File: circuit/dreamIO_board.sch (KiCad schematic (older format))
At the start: 78 parts, among them IC1 TPS61200, P1 BATT, P2 CONN_01X08, P3 CONN_01X08, P4 CONN_01X02, P5 CONN_01X06, P6 gnd_con, P7 CONN_01X03, P8 NO_CASCADE, P9 PixelOut, SW1 SPDT, SW2 RESET, SW3 PRGM, SW4 HCI2, SW5 HCI1, U1 MCP73831, U17 MPU-6050, U2 MICRO-B_USB, U3 UA78M33_SOT223, U4 ESP-12E

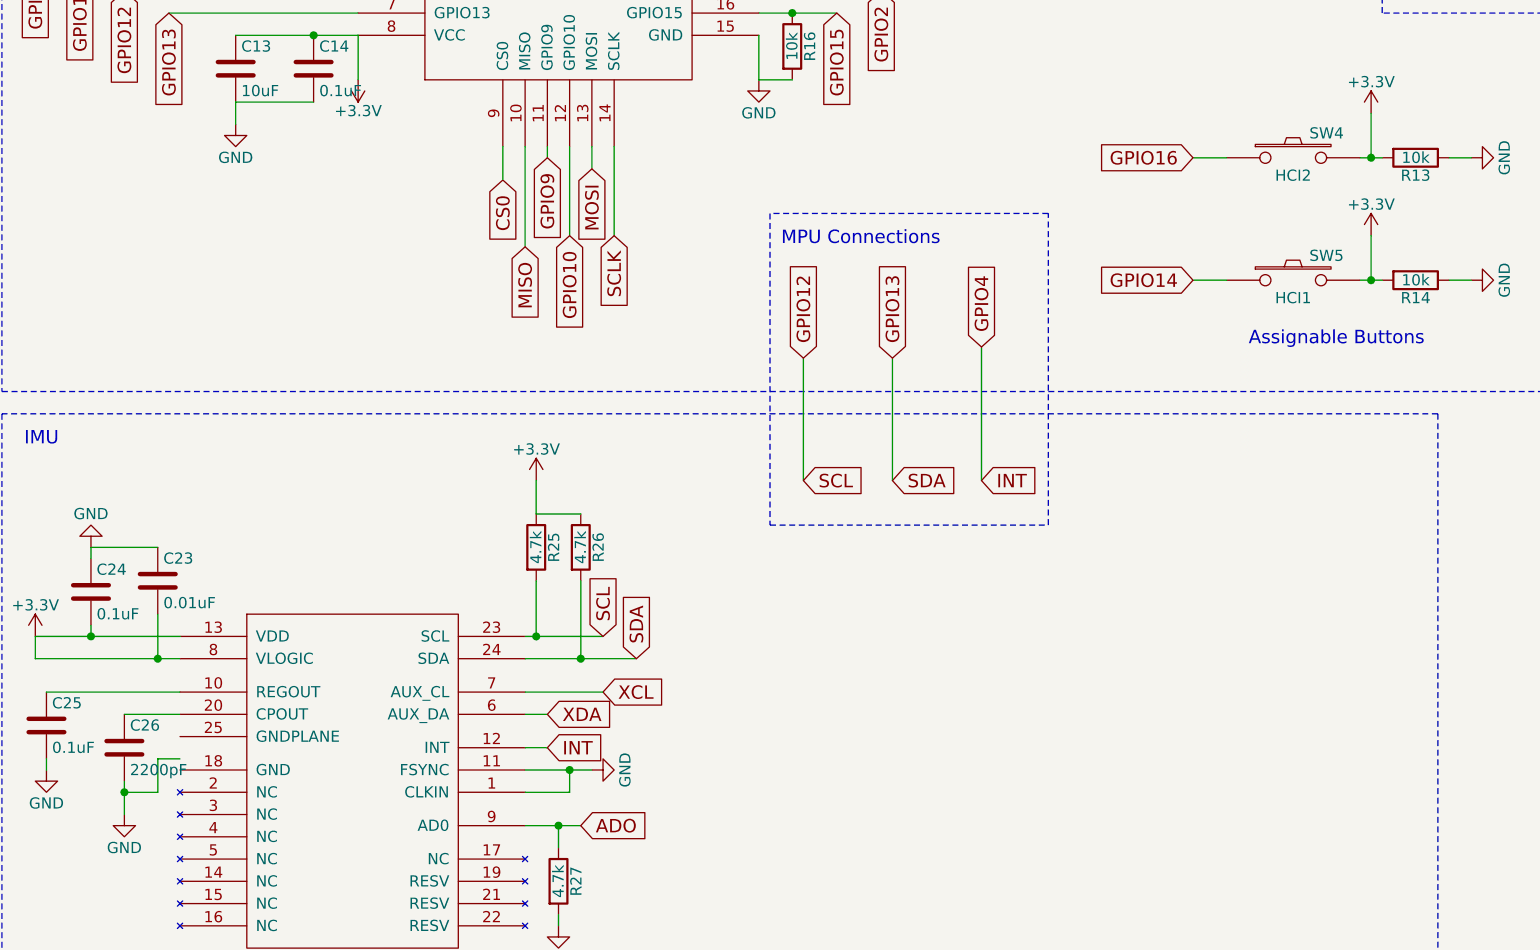
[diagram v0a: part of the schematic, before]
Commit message: changed pinout for MPU6050 to include groundplane under area. started on routing
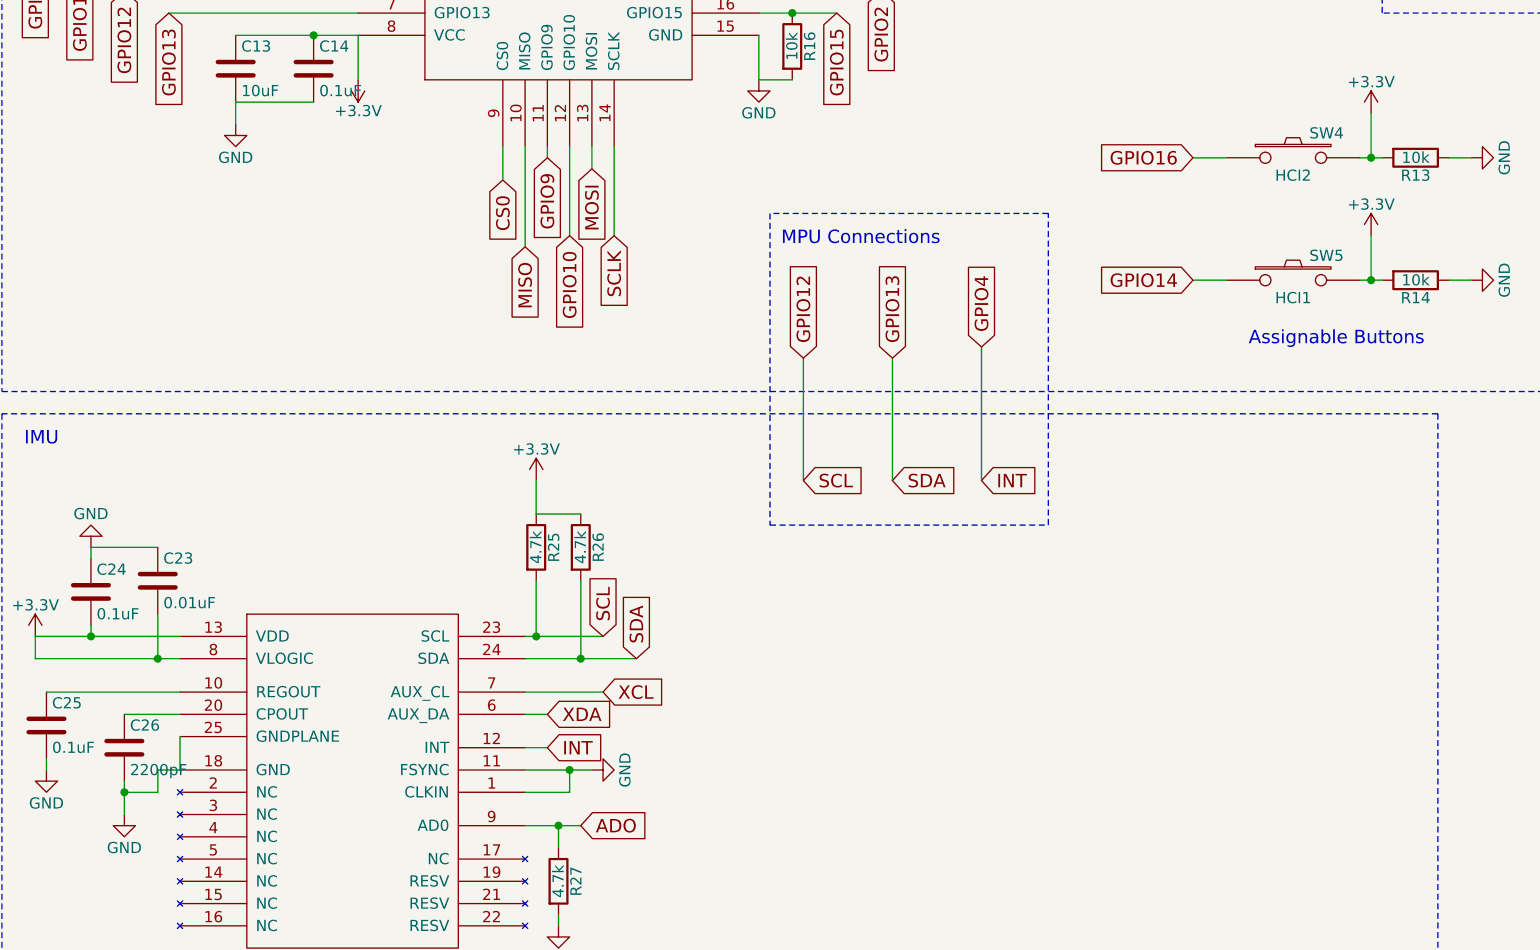
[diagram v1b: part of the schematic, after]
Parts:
- U17: footprint kicad-libraries:QFN-24-4x4-EP -> mpu6050:QFN-24-4x4-EP_steevedit
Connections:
- net GND: now also U17.18 (GND), U17.25 (GNDPLANE)
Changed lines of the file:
@@
 F 0 "U17" H 3150 11700 60  0000 C CNN
 F 1 "MPU-6050" H 2550 11700 60  0000 C CNN
-F 2 "kicad-libraries:QFN-24-4x4-EP" H 2800 12150 60  0001 C CNN
+F 2 "mpu6050:QFN-24-4x4-EP_steevedit" H 2800 12150 60  0001 C CNN
 F 3 "" H 2800 12150 60  0000 C CNN
 	1    2800 12400
@@
 	1900 12300 1750 12300
 Wire Wire Line
-	1900 12150 1900 12300
-Wire Wire Line
-	2000 12150 1900 12150
+	1900 12200 1900 12300
+Wire Wire Line
+	2000 12200 1900 12200
 Wire Wire Line
 	1750 12250 1750 12400
@@
 	7800 9450 7700 9450
 Wire Wire Line
-	7400 9450 7300 9450
+	7300 9450 7400 9450
 $Comp
 L +3.3V #PWR048
@@
 	7800 10000 7700 10000
 Wire Wire Line
-	7400 10000 7300 10000
+	7300 10000 7400 10000
 $Comp
 L +3.3V #PWR050
@@
 Text Notes 6750 2500 0    60   ~ 0
 in case no 3.3v reg
+Wire Wire Line
+	2000 12050 2000 12200
 $EndSCHEMATC

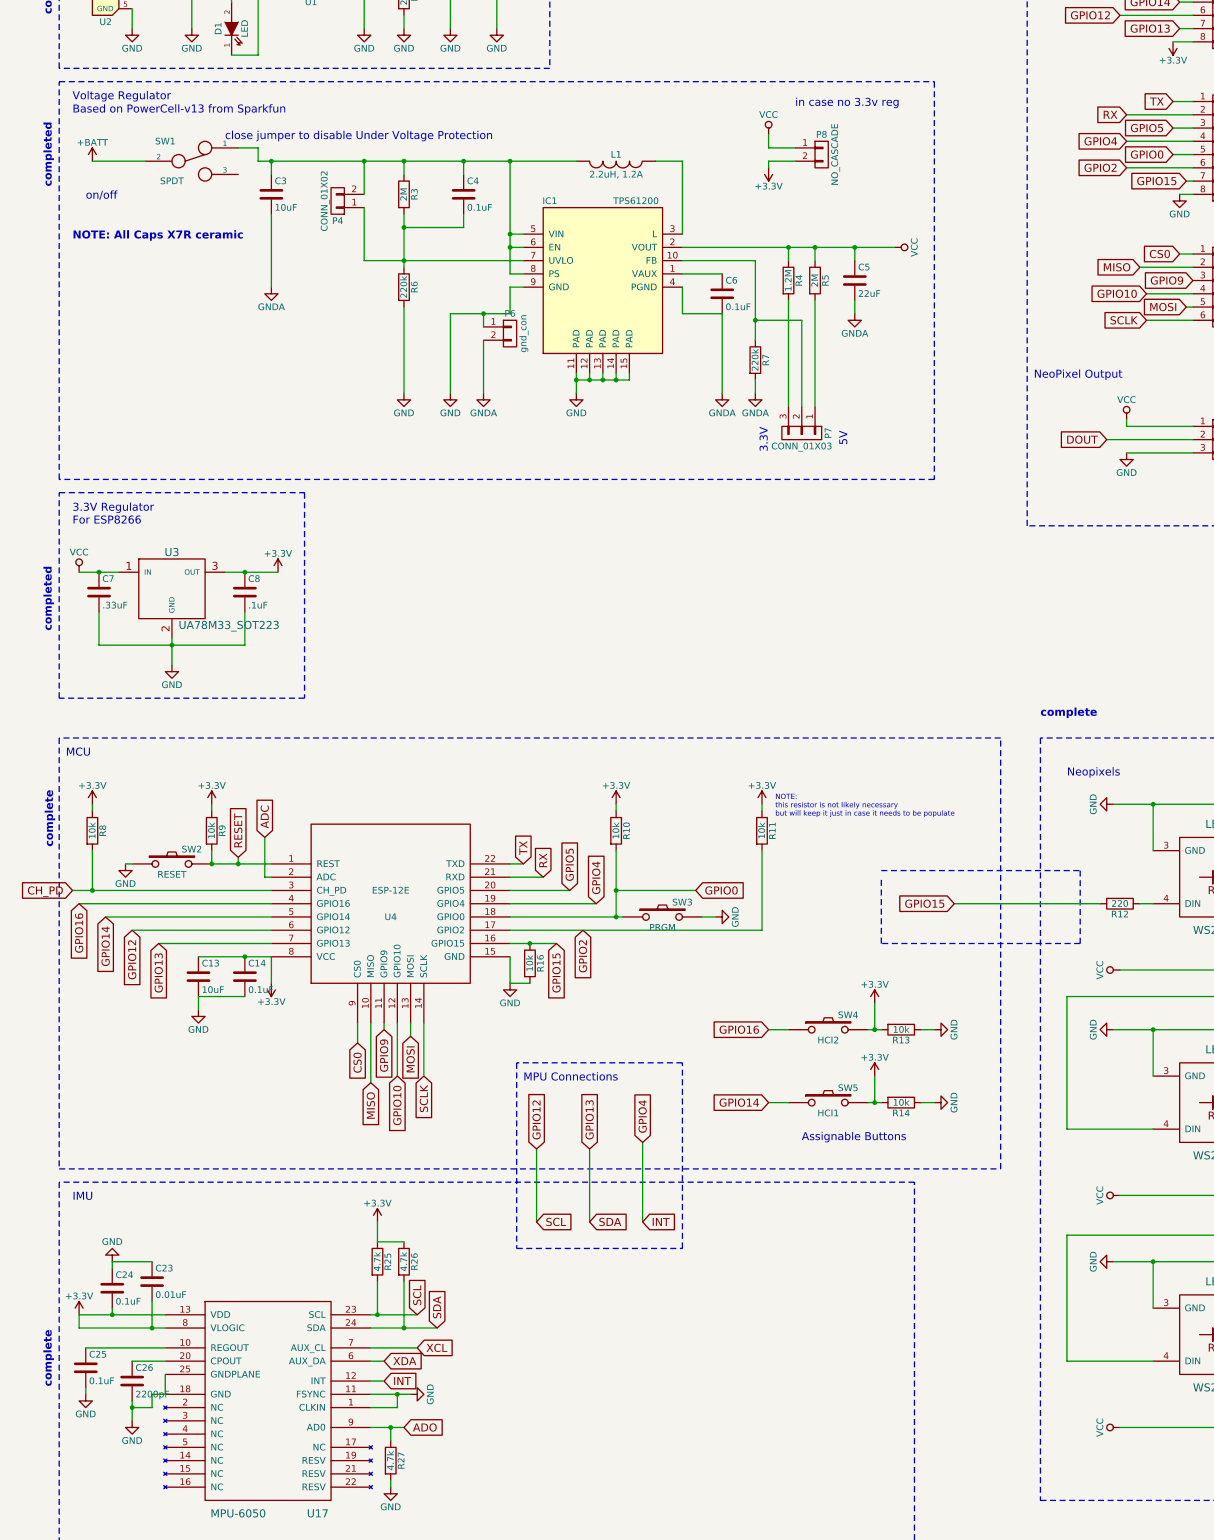
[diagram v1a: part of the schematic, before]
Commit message: removed the 3.3V regulator. The TPS61200 is now the main regulator and will be 5V.
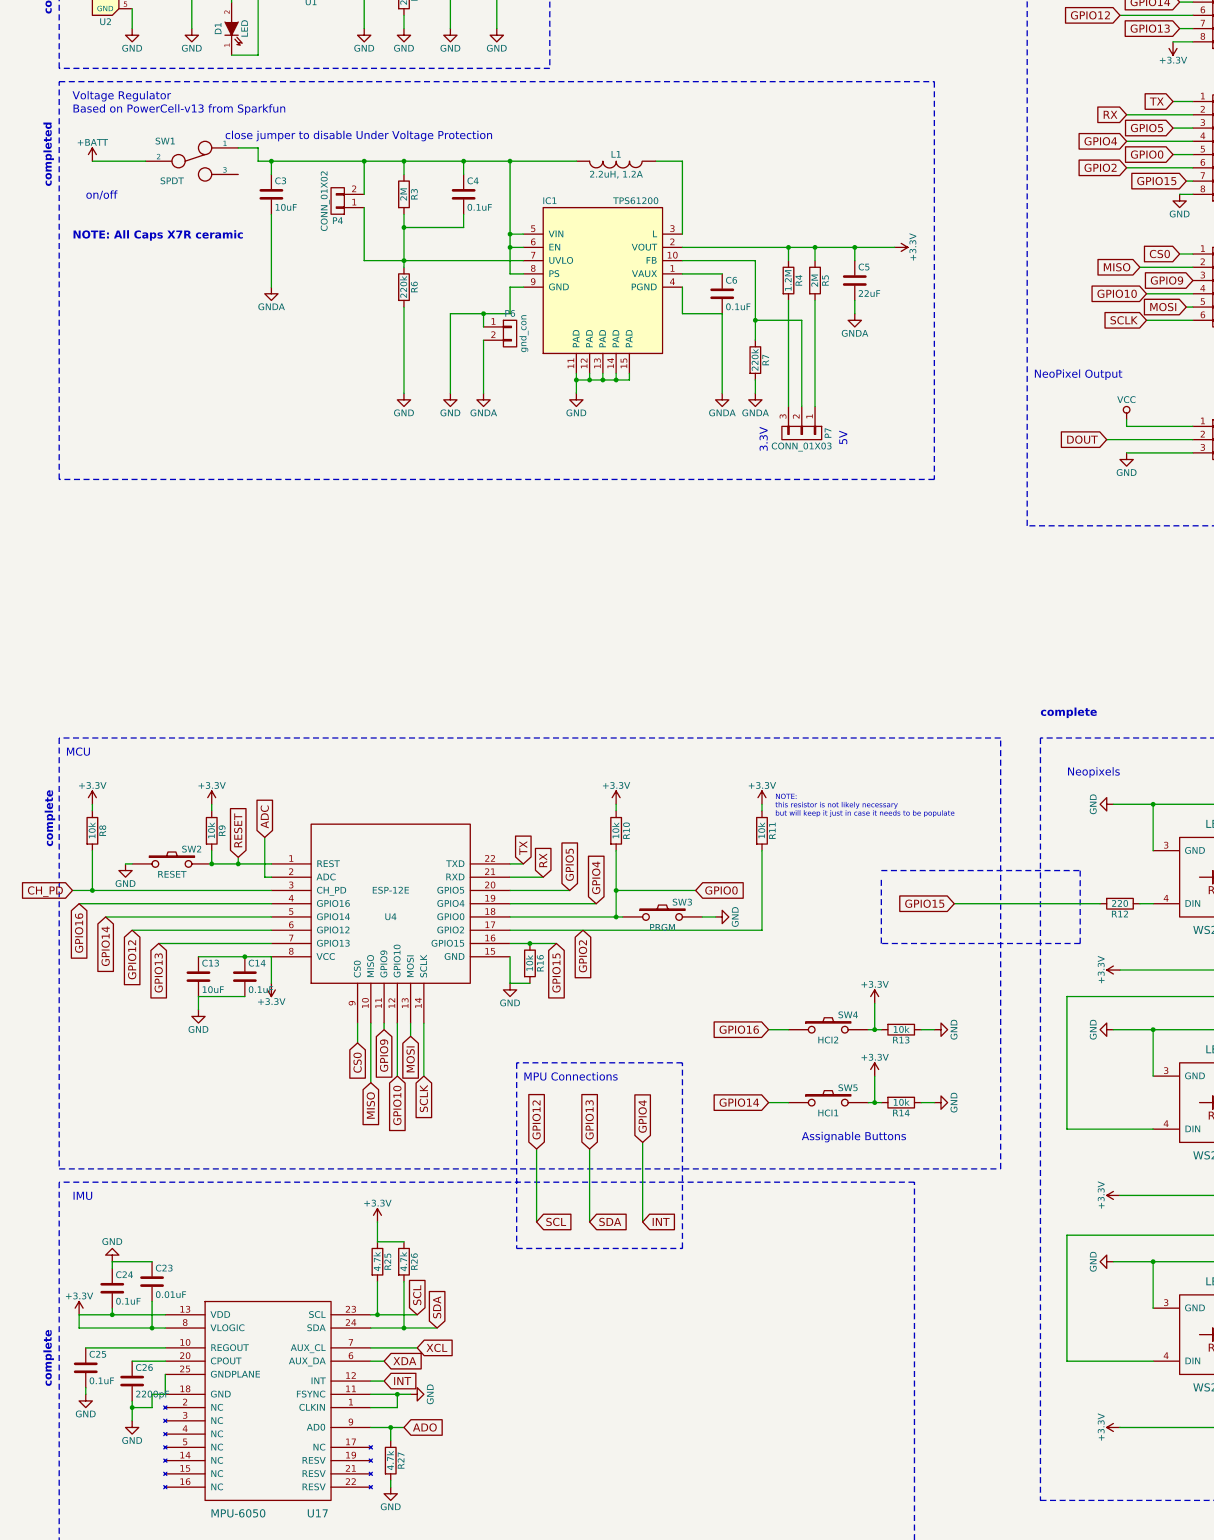
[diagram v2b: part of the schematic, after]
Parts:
- removed C7: .33uF, kicad-libraries:0603, symbol C
- removed C8: .1uF, kicad-libraries:0603, symbol C
- removed P8: NO_CASCADE, _connectors:_Solder_Pad2.54_2, symbol CONN_01X02
- removed U3: UA78M33_SOT223, kicad-libraries:SOT-223, symbol UA78M33_SOT223
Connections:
- net +3V3: now also C10.2, C11.2, C12.2, C15.2, C16.2, C17.2, C18.2, C19.2, C20.2, C21.2, C22.2, C5.1, C9.2, IC1.2 (VOUT), LED1.1 (VCC), LED10.1 (VCC), LED11.1 (VCC), LED12.1 (VCC), LED2.1 (VCC), LED3.1 (VCC), LED4.1 (VCC), LED5.1 (VCC), LED6.1 (VCC), LED7.1 (VCC), LED8.1 (VCC), LED9.1 (VCC), R4.1, R5.1
- net VCC: no longer C10.2, C11.2, C12.2, C15.2, C16.2, C17.2, C18.2, C19.2, C20.2, C21.2, C22.2, C5.1, C9.2, IC1.2 (VOUT), LED1.1 (VCC), LED10.1 (VCC), LED11.1 (VCC), LED12.1 (VCC), LED2.1 (VCC), LED3.1 (VCC), LED4.1 (VCC), LED5.1 (VCC), LED6.1 (VCC), LED7.1 (VCC), LED8.1 (VCC), LED9.1 (VCC), R4.1, R5.1
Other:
- note removed: "3.3V Regulator\nFor ESP8266"
- note removed: "in case no 3.3v reg"

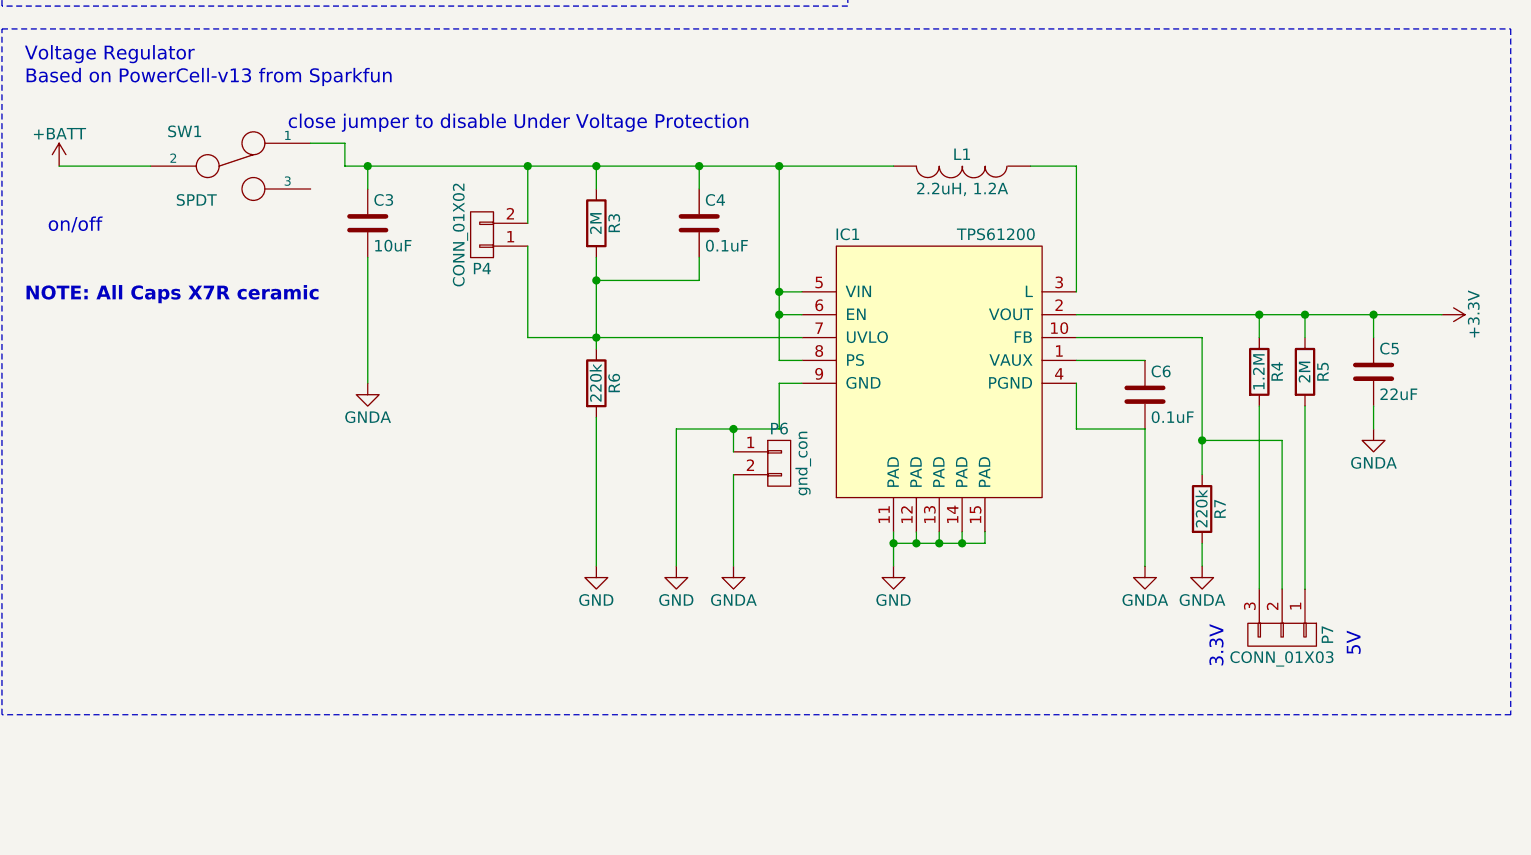
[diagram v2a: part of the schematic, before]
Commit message: added ADC voltage measurement. A voltage resistor of R1 2M and R2 330K keeps the maximum voltage of the battery (4.2V) below the 1V maximum for the analog pin. If the resistor network is not populated the pin remains empty
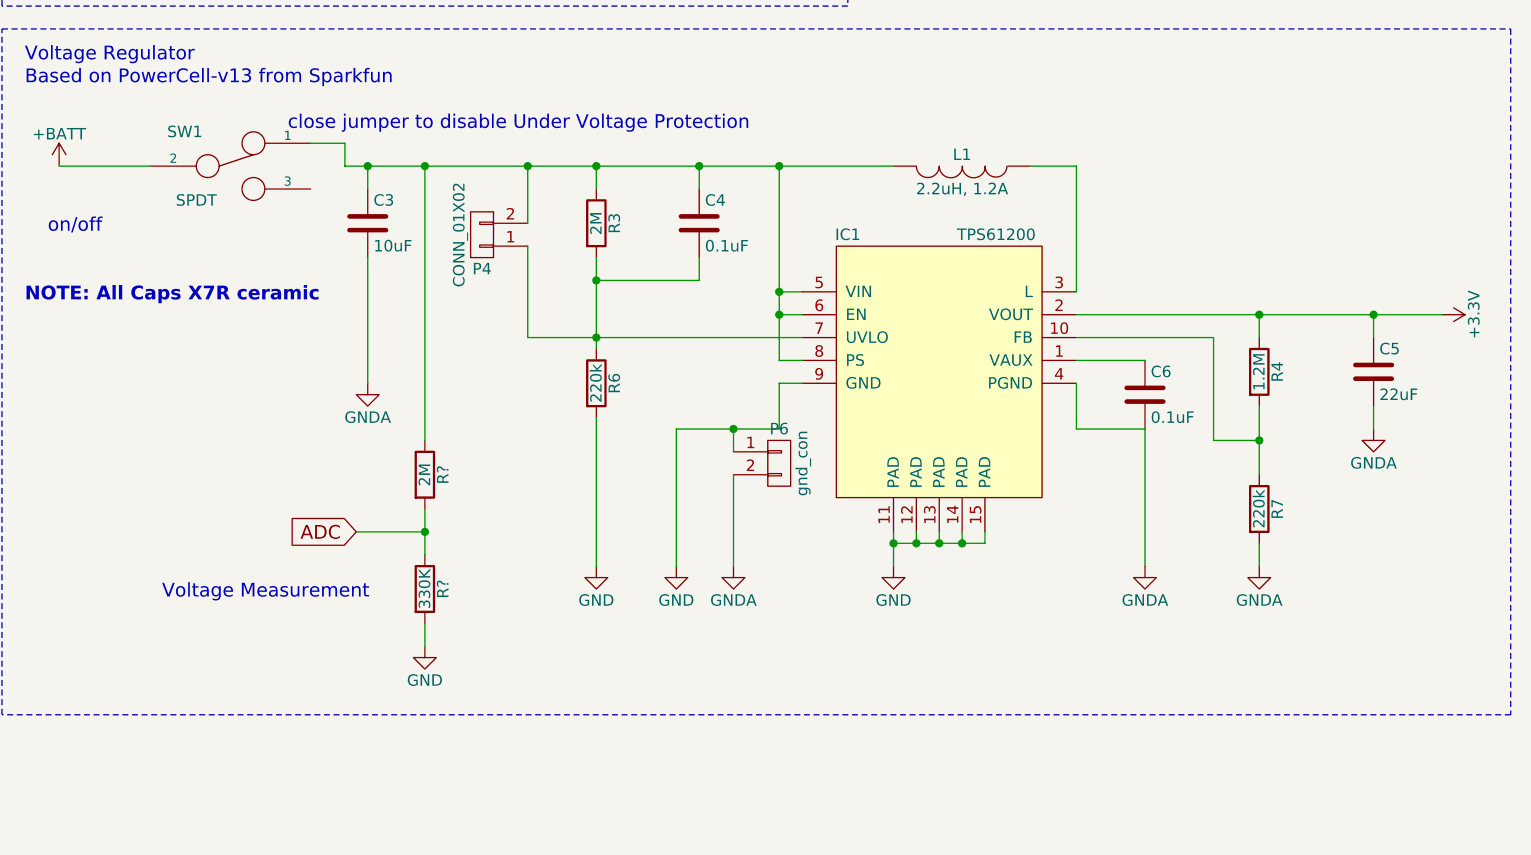
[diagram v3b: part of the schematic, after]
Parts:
- removed P7: CONN_01X03, _connectors:_Solder_Pad2.54_3, symbol CONN_01X03
- removed R5: 2M, kicad-libraries:0603, symbol R
- added R?: 2M, kicad-libraries:0603, symbol R
- added R?: 330K, kicad-libraries:0603, symbol R
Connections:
- net ADC: now also R?.1, R?.2
- net GND: now also R?.2
- net at IC1.10 (FB), R7.1: now also R4.2
- net at C3.1, C4.1, IC1.5 (VIN)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: now also R?.1
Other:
- note added: "Voltage Measurement"
- note removed: "3.3V\n"
- note removed: "5V"
- moved on the sheet: R7
